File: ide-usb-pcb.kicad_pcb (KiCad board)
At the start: 2 copper layers, 4 parts, among them J1 STM32F4_Discovery_Header, J2 Conn_02x20_Odd_Even, U1 TXS0108EPW, U2 TXS0108EPW

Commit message: Add power & GND nets
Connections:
- J1 pad 1: Net-(J1-Pad1) -> GND
- J1 pad 100: Net-(J1-Pad100) -> GND
- J1 pad 2: Net-(J1-Pad2) -> GND
- J1 pad 49: Net-(J1-Pad49) -> GND
- J1 pad 50: Net-(J1-Pad50) -> GND
- J1 pad 51: Net-(J1-Pad51) -> GND
- J1 pad 52: Net-(J1-Pad52) -> GND
- J1 pad 96: Net-(J1-Pad96) -> +3V3
- J1 pad 99: Net-(J1-Pad99) -> GND
- J2 pad 19: Net-(J2-Pad19) -> GND
- J2 pad 2: Net-(J2-Pad2) -> GND
- J2 pad 22: Net-(J2-Pad22) -> GND
- J2 pad 24: Net-(J2-Pad24) -> GND
- J2 pad 26: Net-(J2-Pad26) -> GND
- J2 pad 30: Net-(J2-Pad30) -> GND
- J2 pad 40: Net-(J2-Pad40) -> GND
- U1 pad 11: Net-(U1-Pad11) -> GND
- U1 pad 19: Net-(U1-Pad19) -> +5V
- U1 pad 2: Net-(U1-Pad2) -> +3V3
- U2 pad 11: Net-(U2-Pad11) -> GND
- U2 pad 19: Net-(U2-Pad19) -> +5V
- U2 pad 2: Net-(U2-Pad2) -> +3V3

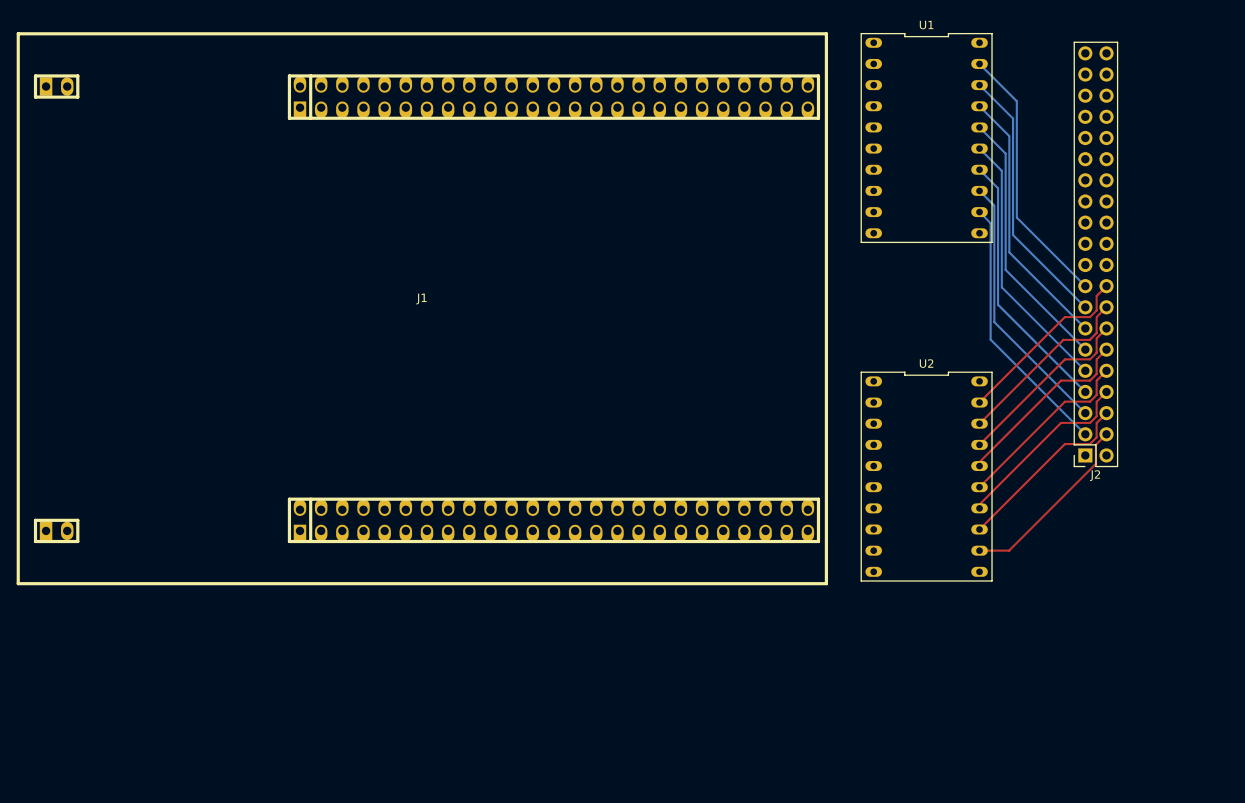
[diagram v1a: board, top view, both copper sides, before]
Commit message: Add termination resistors
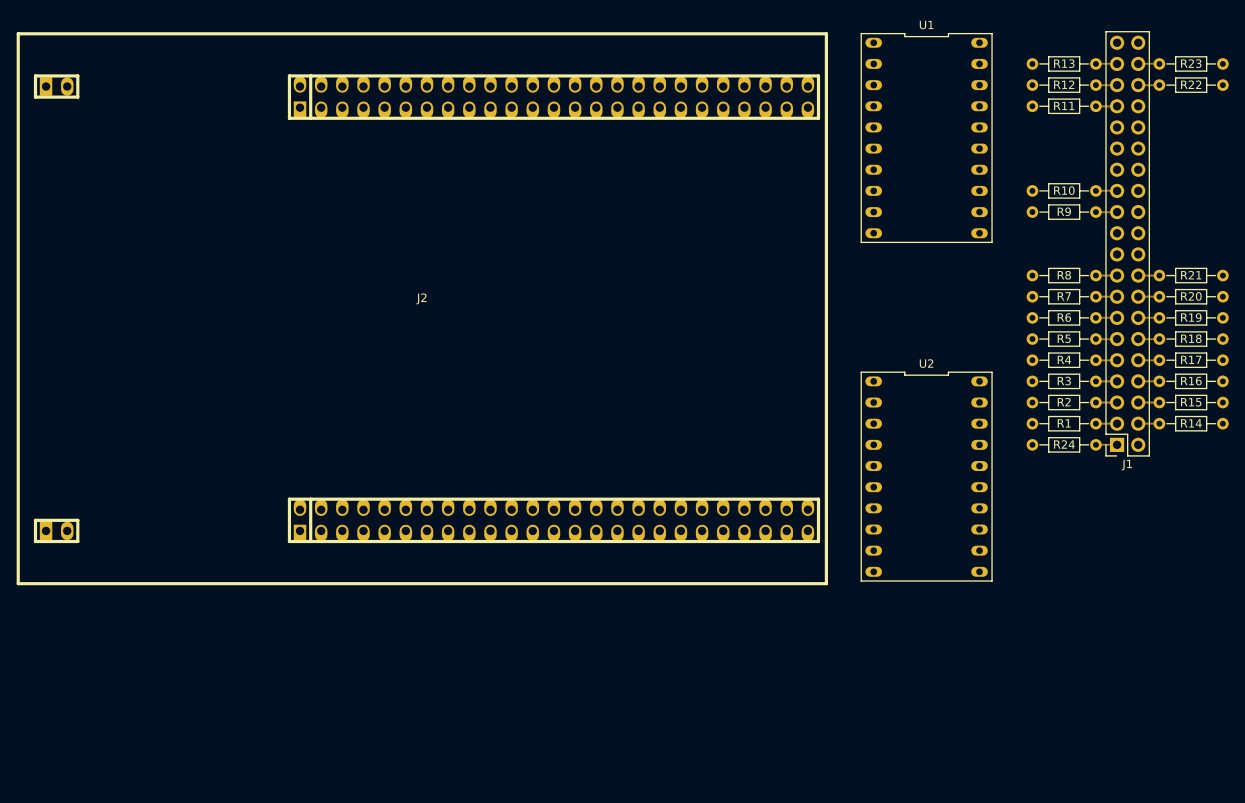
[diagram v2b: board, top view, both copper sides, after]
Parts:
- added R1: 33, Resistors_THT:R_Axial_DIN0204_L3.6mm_D1.6mm_P7.62mm_Horizontal, F.Cu at (156.2, 66.0)
- added R10: 22, Resistors_THT:R_Axial_DIN0204_L3.6mm_D1.6mm_P7.62mm_Horizontal, F.Cu at (156.2, 38.1)
- added R11: 33, Resistors_THT:R_Axial_DIN0204_L3.6mm_D1.6mm_P7.62mm_Horizontal, F.Cu at (156.2, 27.9)
- added R12: 33, Resistors_THT:R_Axial_DIN0204_L3.6mm_D1.6mm_P7.62mm_Horizontal, F.Cu at (156.2, 25.4)
- added R13: 33, Resistors_THT:R_Axial_DIN0204_L3.6mm_D1.6mm_P7.62mm_Horizontal, F.Cu at (156.2, 22.9)
- added R14: 33, Resistors_THT:R_Axial_DIN0204_L3.6mm_D1.6mm_P7.62mm_Horizontal, F.Cu at (171.4, 66.0)
- added R15: 33, Resistors_THT:R_Axial_DIN0204_L3.6mm_D1.6mm_P7.62mm_Horizontal, F.Cu at (171.4, 63.5)
- added R16: 33, Resistors_THT:R_Axial_DIN0204_L3.6mm_D1.6mm_P7.62mm_Horizontal, F.Cu at (171.4, 61.0)
- added R17: 33, Resistors_THT:R_Axial_DIN0204_L3.6mm_D1.6mm_P7.62mm_Horizontal, F.Cu at (171.4, 58.4)
- added R18: 33, Resistors_THT:R_Axial_DIN0204_L3.6mm_D1.6mm_P7.62mm_Horizontal, F.Cu at (171.4, 55.9)
- added R19: 33, Resistors_THT:R_Axial_DIN0204_L3.6mm_D1.6mm_P7.62mm_Horizontal, F.Cu at (171.4, 53.3)
- added R2: 33, Resistors_THT:R_Axial_DIN0204_L3.6mm_D1.6mm_P7.62mm_Horizontal, F.Cu at (156.2, 63.5)
- added R20: 33, Resistors_THT:R_Axial_DIN0204_L3.6mm_D1.6mm_P7.62mm_Horizontal, F.Cu at (171.4, 50.8)
- added R21: 33, Resistors_THT:R_Axial_DIN0204_L3.6mm_D1.6mm_P7.62mm_Horizontal, F.Cu at (171.4, 48.3)
- added R22: 33, Resistors_THT:R_Axial_DIN0204_L3.6mm_D1.6mm_P7.62mm_Horizontal, F.Cu at (171.4, 25.4)
- added R23: 33, Resistors_THT:R_Axial_DIN0204_L3.6mm_D1.6mm_P7.62mm_Horizontal, F.Cu at (171.4, 22.9)
- added R24: 33, Resistors_THT:R_Axial_DIN0204_L3.6mm_D1.6mm_P7.62mm_Horizontal, F.Cu at (156.2, 68.6)
- added R3: 33, Resistors_THT:R_Axial_DIN0204_L3.6mm_D1.6mm_P7.62mm_Horizontal, F.Cu at (156.2, 61.0)
- added R4: 33, Resistors_THT:R_Axial_DIN0204_L3.6mm_D1.6mm_P7.62mm_Horizontal, F.Cu at (156.2, 58.4)
- added R5: 33, Resistors_THT:R_Axial_DIN0204_L3.6mm_D1.6mm_P7.62mm_Horizontal, F.Cu at (156.2, 55.9)
- added R6: 33, Resistors_THT:R_Axial_DIN0204_L3.6mm_D1.6mm_P7.62mm_Horizontal, F.Cu at (156.2, 53.3)
- added R7: 33, Resistors_THT:R_Axial_DIN0204_L3.6mm_D1.6mm_P7.62mm_Horizontal, F.Cu at (156.2, 50.8)
- added R8: 33, Resistors_THT:R_Axial_DIN0204_L3.6mm_D1.6mm_P7.62mm_Horizontal, F.Cu at (156.2, 48.3)
- added R9: 22, Resistors_THT:R_Axial_DIN0204_L3.6mm_D1.6mm_P7.62mm_Horizontal, F.Cu at (156.2, 40.6)
- moved J1 4.02 mm to (158.8, 68.6)
- renumbered J2 to J1, J1 to J2
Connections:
- J1 pad 1: /RESET -> Net-(J1-Pad1)
- J1 pad 10: /DD11B -> Net-(J1-Pad10)
- J1 pad 11: /DD3B -> Net-(J1-Pad11)
- J1 pad 12: /DD12B -> Net-(J1-Pad12)
- J1 pad 13: /DD2B -> Net-(J1-Pad13)
- J1 pad 14: /DD13B -> Net-(J1-Pad14)
- J1 pad 15: /DD1B -> Net-(J1-Pad15)
- J1 pad 16: /DD14B -> Net-(J1-Pad16)
- J1 pad 17: /DD0B -> Net-(J1-Pad17)
- J1 pad 18: /DD15B -> Net-(J1-Pad18)
- J1 pad 20: Net-(J2-Pad20) -> (no net)
- J1 pad 21: Net-(J2-Pad21) -> (no net)
- J1 pad 23: /DIOW -> Net-(J1-Pad23)
- J1 pad 25: /DIOR -> Net-(J1-Pad25)
- J1 pad 27: Net-(J2-Pad27) -> (no net)
- J1 pad 28: Net-(J2-Pad28) -> (no net)
- J1 pad 29: Net-(J2-Pad29) -> (no net)
- J1 pad 3: /DD7B -> Net-(J1-Pad3)
- J1 pad 31: Net-(J2-Pad31) -> (no net)
- J1 pad 32: Net-(J2-Pad32) -> (no net)
- J1 pad 33: /DA1 -> Net-(J1-Pad33)
- J1 pad 34: Net-(J2-Pad34) -> (no net)
- J1 pad 35: /DA0 -> Net-(J1-Pad35)
- J1 pad 36: /DA2 -> Net-(J1-Pad36)
- J1 pad 37: /CS0 -> Net-(J1-Pad37)
- J1 pad 38: /CS1 -> Net-(J1-Pad38)
- J1 pad 39: Net-(J2-Pad39) -> (no net)
- J1 pad 4: /DD8B -> Net-(J1-Pad4)
- J1 pad 5: /DD6B -> Net-(J1-Pad5)
- J1 pad 6: /DD9B -> Net-(J1-Pad6)
- J1 pad 7: /DD5B -> Net-(J1-Pad7)
- J1 pad 8: /DD10B -> Net-(J1-Pad8)
- J1 pad 9: /DD4B -> Net-(J1-Pad9)
- J2 pad 10: Net-(J1-Pad10) -> (no net)
- J2 pad 11: Net-(J1-Pad11) -> (no net)
- J2 pad 12: Net-(J1-Pad12) -> (no net)
- J2 pad 13: Net-(J1-Pad13) -> (no net)
- J2 pad 14: Net-(J1-Pad14) -> (no net)
- J2 pad 15: Net-(J1-Pad15) -> (no net)
- J2 pad 16: Net-(J1-Pad16) -> (no net)
- J2 pad 17: Net-(J1-Pad17) -> (no net)
- J2 pad 18: Net-(J1-Pad18) -> (no net)
- J2 pad 19: Net-(J1-Pad19) -> (no net)
- J2 pad 21: Net-(J1-Pad21) -> (no net)
- J2 pad 22: Net-(J1-Pad22) -> (no net)
- J2 pad 23: Net-(J1-Pad23) -> (no net)
- J2 pad 24: Net-(J1-Pad24) -> (no net)
- J2 pad 3: Net-(J1-Pad3) -> (no net)
- J2 pad 34: Net-(J1-Pad34) -> (no net)
- J2 pad 35: Net-(J1-Pad35) -> (no net)
- J2 pad 36: Net-(J1-Pad36) -> (no net)
- J2 pad 37: Net-(J1-Pad37) -> (no net)
- J2 pad 38: Net-(J1-Pad38) -> (no net)
- J2 pad 4: Net-(J1-Pad4) -> (no net)
- J2 pad 43: Net-(J1-Pad43) -> (no net)
- J2 pad 44: Net-(J1-Pad44) -> (no net)
- J2 pad 45: Net-(J1-Pad45) -> (no net)
- J2 pad 46: Net-(J1-Pad46) -> (no net)
- J2 pad 47: Net-(J1-Pad47) -> (no net)
- J2 pad 48: Net-(J1-Pad48) -> (no net)
- J2 pad 5: Net-(J1-Pad5) -> (no net)
- J2 pad 53: Net-(J1-Pad53) -> (no net)
- J2 pad 54: Net-(J1-Pad54) -> (no net)
- J2 pad 57: Net-(J1-Pad57) -> (no net)
- J2 pad 58: Net-(J1-Pad58) -> (no net)
- J2 pad 59: Net-(J1-Pad59) -> (no net)
- J2 pad 6: Net-(J1-Pad6) -> (no net)
- J2 pad 60: Net-(J1-Pad60) -> (no net)
- J2 pad 61: Net-(J1-Pad61) -> (no net)
- J2 pad 62: Net-(J1-Pad62) -> (no net)
- J2 pad 63: Net-(J1-Pad63) -> (no net)
- J2 pad 65: Net-(J1-Pad65) -> (no net)
- J2 pad 7: Net-(J1-Pad7) -> (no net)
- J2 pad 70: Net-(J1-Pad70) -> (no net)
- J2 pad 71: Net-(J1-Pad71) -> (no net)
- J2 pad 72: Net-(J1-Pad72) -> (no net)
- J2 pad 73: Net-(J1-Pad73) -> (no net)
- J2 pad 74: Net-(J1-Pad74) -> (no net)
- J2 pad 75: Net-(J1-Pad75) -> (no net)
- J2 pad 76: Net-(J1-Pad76) -> (no net)
- J2 pad 77: Net-(J1-Pad77) -> (no net)
- J2 pad 78: Net-(J1-Pad78) -> (no net)
- J2 pad 79: Net-(J1-Pad79) -> (no net)
- J2 pad 8: Net-(J1-Pad8) -> (no net)
- J2 pad 80: Net-(J1-Pad80) -> (no net)
- J2 pad 82: Net-(J1-Pad82) -> (no net)
- J2 pad 83: Net-(J1-Pad83) -> (no net)
- J2 pad 84: Net-(J1-Pad84) -> (no net)
- J2 pad 85: Net-(J1-Pad85) -> (no net)
- J2 pad 86: Net-(J1-Pad86) -> (no net)
- J2 pad 9: Net-(J1-Pad9) -> (no net)
- J2 pad 90: Net-(J1-Pad90) -> (no net)
- J2 pad 91: Net-(J1-Pad91) -> (no net)
- J2 pad 92: Net-(J1-Pad92) -> (no net)
- J2 pad 93: Net-(J1-Pad93) -> (no net)
- J2 pad 94: Net-(J1-Pad94) -> (no net)
- J2 pad 95: Net-(J1-Pad95) -> (no net)
- J2 pad 97: Net-(J1-Pad97) -> (no net)
- J2 pad 98: Net-(J1-Pad98) -> (no net)
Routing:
- net /DD7B: track 31.9 -> 0.00 mm
- net /DD3B: track 31.9 -> 0.00 mm
- net /DD2B: track 31.9 -> 0.00 mm
- net /DD1B: track 31.9 -> 0.00 mm
- net /DD0B: track 31.9 -> 0.00 mm
- net /DD6B: track 31.9 -> 0.00 mm
- net /DD5B: track 31.9 -> 0.00 mm
- net /DD4B: track 31.9 -> 0.00 mm
- net /DD8B: track 22.4 -> 0.00 mm
- net /DD14B: track 22.1 -> 0.00 mm
- net /DD9B: track 22.0 -> 0.00 mm
- net /DD15B: track 22.0 -> 0.00 mm
- net /DD13B: track 22.0 -> 0.00 mm
- net /DD11B: track 22.0 -> 0.00 mm
- net /DD12B: track 22.3 -> 0.47 mm
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
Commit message: 1st attempt at routing, excl ground and power
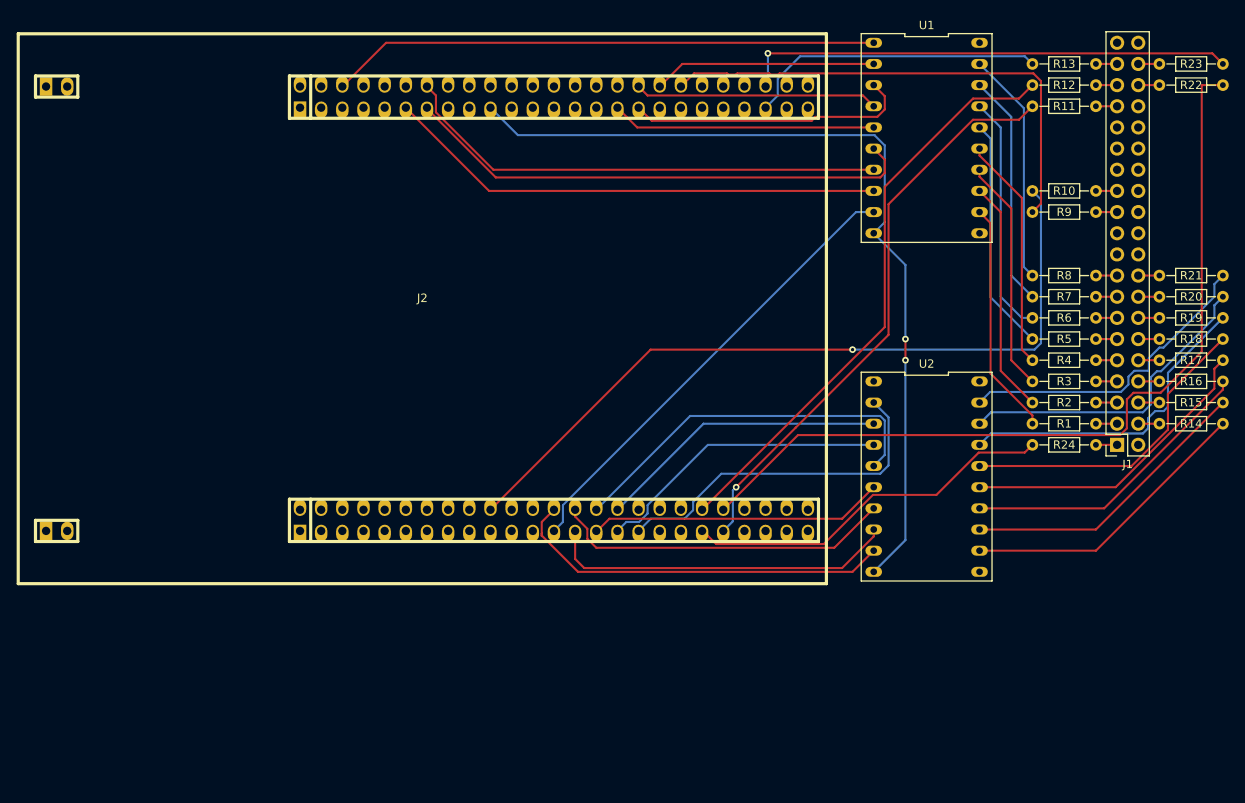
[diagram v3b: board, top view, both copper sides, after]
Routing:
- net /OE: track 0.00 -> 104.1 mm, vias 0 -> 2
- net /DA2: track 0.00 -> 101.9 mm
- net /DIOR: track 0.00 -> 93.1 mm, vias 0 -> 1
- net /DA0: track 0.00 -> 70.6 mm
- net /DA1: track 0.00 -> 69.6 mm, vias 0 -> 1
- net +3V3: track 0.00 -> 66.0 mm
- net /DD4A: track 0.00 -> 62.2 mm
- net /DIOW: track 0.00 -> 60.6 mm
- net /DD6A: track 0.00 -> 60.3 mm
- net /CS1: track 0.00 -> 59.2 mm, vias 0 -> 1
- net /DD5A: track 0.00 -> 58.9 mm
- net /DD7A: track 0.00 -> 55.4 mm
- net /DD8A: track 0.00 -> 46.7 mm
- net /DD12A: track 0.00 -> 46.0 mm
- net /RESET: track 0.00 -> 45.2 mm
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
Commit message: New smaller and (maybe) cleaner PCB design
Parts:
- moved R23 131.4 mm to (45.7, 61.0), turned to 270 degrees
- moved R22 128.2 mm to (48.3, 61.0), turned to 270 degrees
- moved R13 122.7 mm to (45.7, 76.2), turned to 270 degrees
- moved R12 119.3 mm to (48.3, 76.2), turned to 270 degrees
- moved R11 115.9 mm to (50.8, 76.2), turned to 270 degrees
- moved R10 102.6 mm to (61.0, 76.2), turned to 270 degrees
- moved R21 101.1 mm to (71.1, 61.0), turned to 270 degrees
- moved R9 99.3 mm to (63.5, 76.2), turned to 270 degrees
- moved R20 98.3 mm to (73.7, 61.0), turned to 270 degrees
- moved R19 95.6 mm to (76.2, 61.0), turned to 270 degrees
- moved R18 92.8 mm to (78.7, 61.0), turned to 270 degrees
- moved R17 90.2 mm to (81.3, 61.0), turned to 270 degrees
- moved R8 89.6 mm to (71.1, 76.2), turned to 270 degrees
- moved R16 87.6 mm to (83.8, 61.0), turned to 270 degrees
- moved R7 86.4 mm to (73.7, 76.2), turned to 270 degrees
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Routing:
- net +3V3: track 66.0 -> 195.7 mm, vias 0 -> 3
- net /CS0: track 36.2 -> 110.2 mm, vias 0 -> 1
- net /DD7A: track 55.4 -> 0.00 mm
- net /DIOR: track 93.1 -> 38.1 mm, vias 1 -> 0
- net /RESET: track 45.2 -> 0.00 mm
- net /DD0B: track 28.0 -> 69.2 mm
- net /DD1B: track 28.0 -> 61.4 mm
- net /DD15A: track 42.1 -> 12.6 mm
- net /CS1: track 59.2 -> 88.5 mm
- net /DIOW: track 60.6 -> 88.7 mm
- net /DD2B: track 28.8 -> 55.8 mm
- net /DD6A: track 60.3 -> 34.4 mm
- net /DD4A: track 62.2 -> 36.9 mm
- net /DD14A: track 35.0 -> 10.8 mm
- net /DD3B: track 28.0 -> 50.3 mm
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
